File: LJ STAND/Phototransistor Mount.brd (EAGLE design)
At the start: 160 x 100 mm, 3 parts

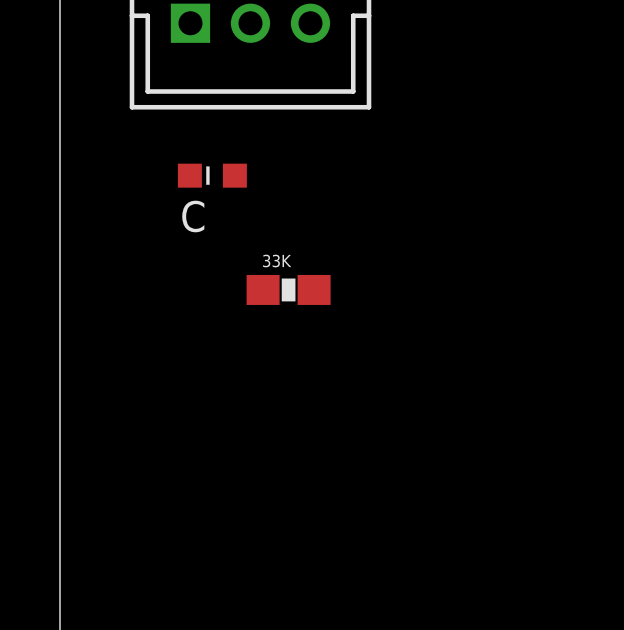
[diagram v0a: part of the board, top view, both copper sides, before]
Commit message: Gyro MPU9250 boards
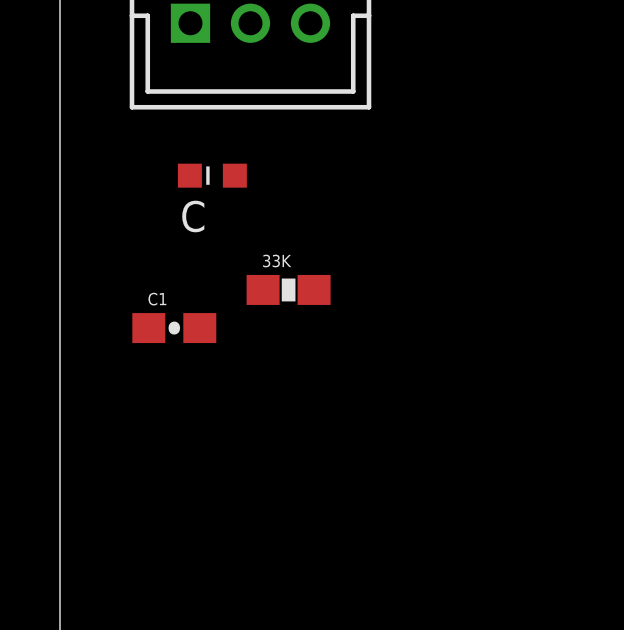
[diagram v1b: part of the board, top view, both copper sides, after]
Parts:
- added C1: 0.1uF, SparkFun-Capacitors:0603-CAP
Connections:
- net N$2: now also C1.2
- net OUT: now also C1.1
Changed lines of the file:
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@@
 <element name="CN1" library="jst-ph" library_urn="urn:adsk.eagle:library:1951258" package="B3B-PH-K-S" package3d_urn="urn:adsk.eagle:package:1951338/1" value="" x="6.35" y="24.13"/>
 <element name="U$1" library="phototransitor-ALS-PT19-315CL177TR8" library_urn="urn:adsk.eagle:library:1968580" package="SMD" package3d_urn="urn:adsk.eagle:package:1968583/2" value="ALS" x="5.08" y="19.05"/>
+<element name="C1" library="SparkFun-Capacitors" package="0603-CAP" value="0.1uF" x="3.81" y="13.97"/>
 </elements>
 <signals>
@@
 <contactref element="33K" pad="2"/>
 <contactref element="CN1" pad="2"/>
+<contactref element="C1" pad="1"/>
 <wire x1="5.83" y1="19.05" x2="6.35" y2="24.13" width="0" layer="19" extent="1-1"/>
 <wire x1="8.47" y1="15.24" x2="5.83" y2="19.05" width="0" layer="19" extent="1-1"/>
+<wire x1="2.96" y1="13.97" x2="8.47" y2="15.24" width="0" layer="19" extent="1-1"/>
 </signal>
 <signal name="N$1">
@@
 <contactref element="33K" pad="1"/>
 <contactref element="CN1" pad="1"/>
+<contactref element="C1" pad="2"/>
 <wire x1="6.77" y1="15.24" x2="4.35" y2="24.13" width="0" layer="19" extent="1-1"/>
+<wire x1="4.66" y1="13.97" x2="6.77" y2="15.24" width="0" layer="19" extent="1-1"/>
 </signal>
 </signals>
